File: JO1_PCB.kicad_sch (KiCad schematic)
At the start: 13 parts, among them J1 CN8, J10 ESC_PWM, J11 CAN_WCMCU-1051_BLUEPILL, J2 CN7, J3 CN9, J4 CN10, J5 MPU-6050, J6 CAN_WCMCU-1051_NUCLEO, J7 SERVO, J8 DC_MOTOR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

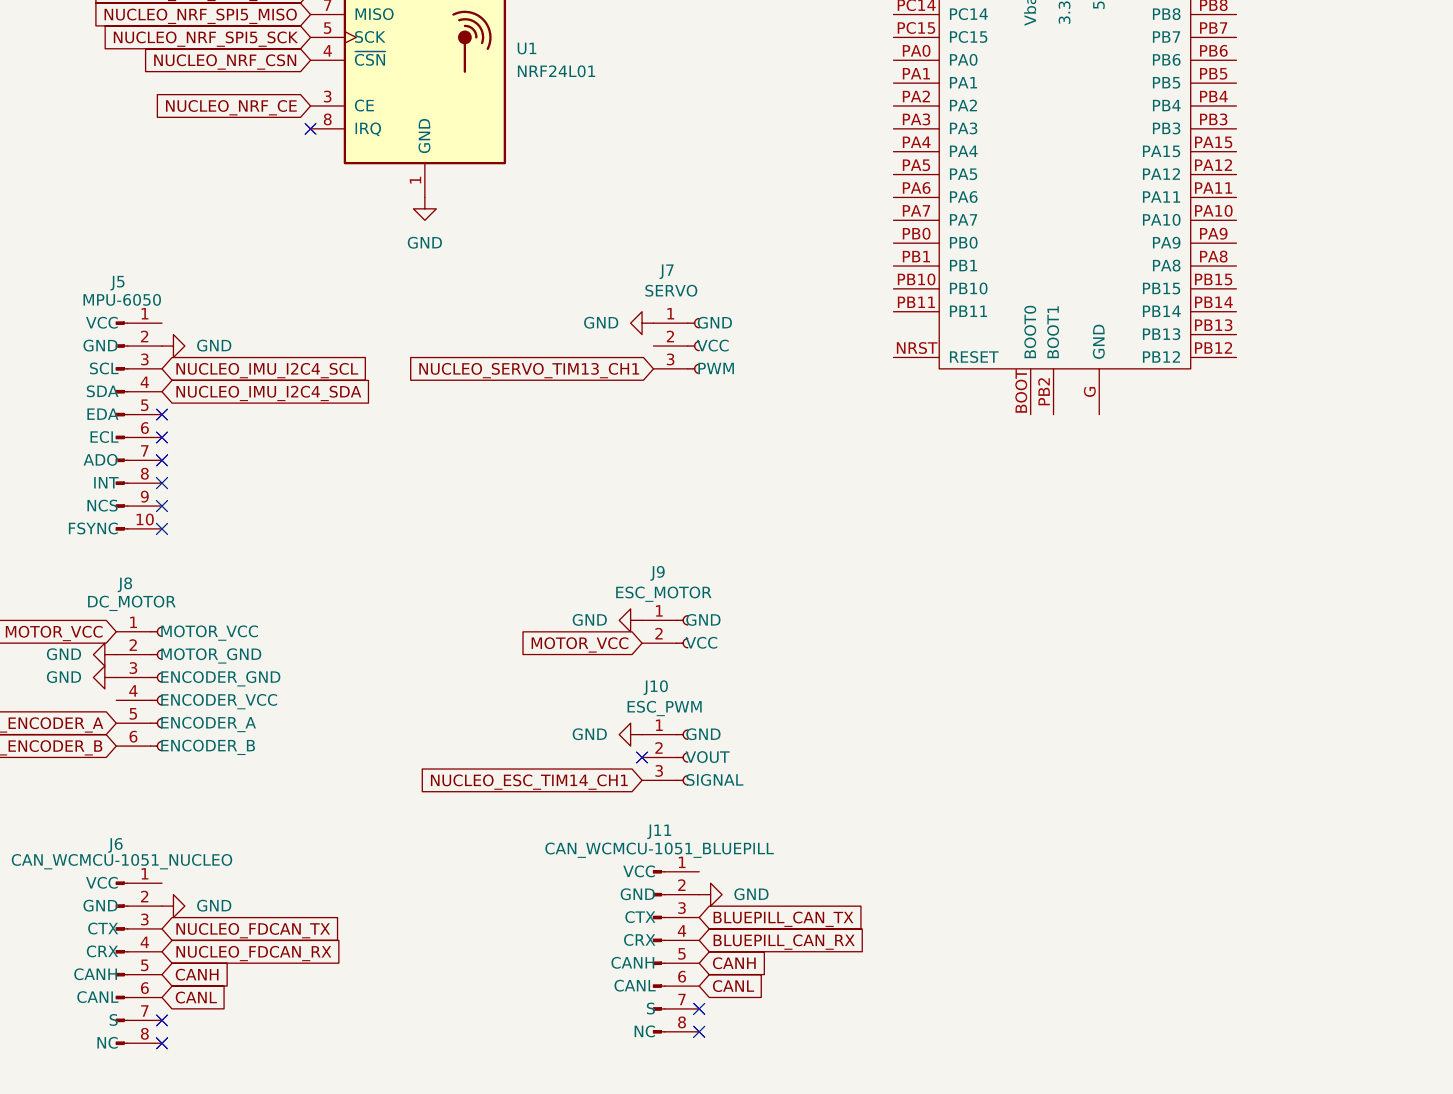
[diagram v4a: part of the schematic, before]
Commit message: Added CAN transceiver for Blue Pill
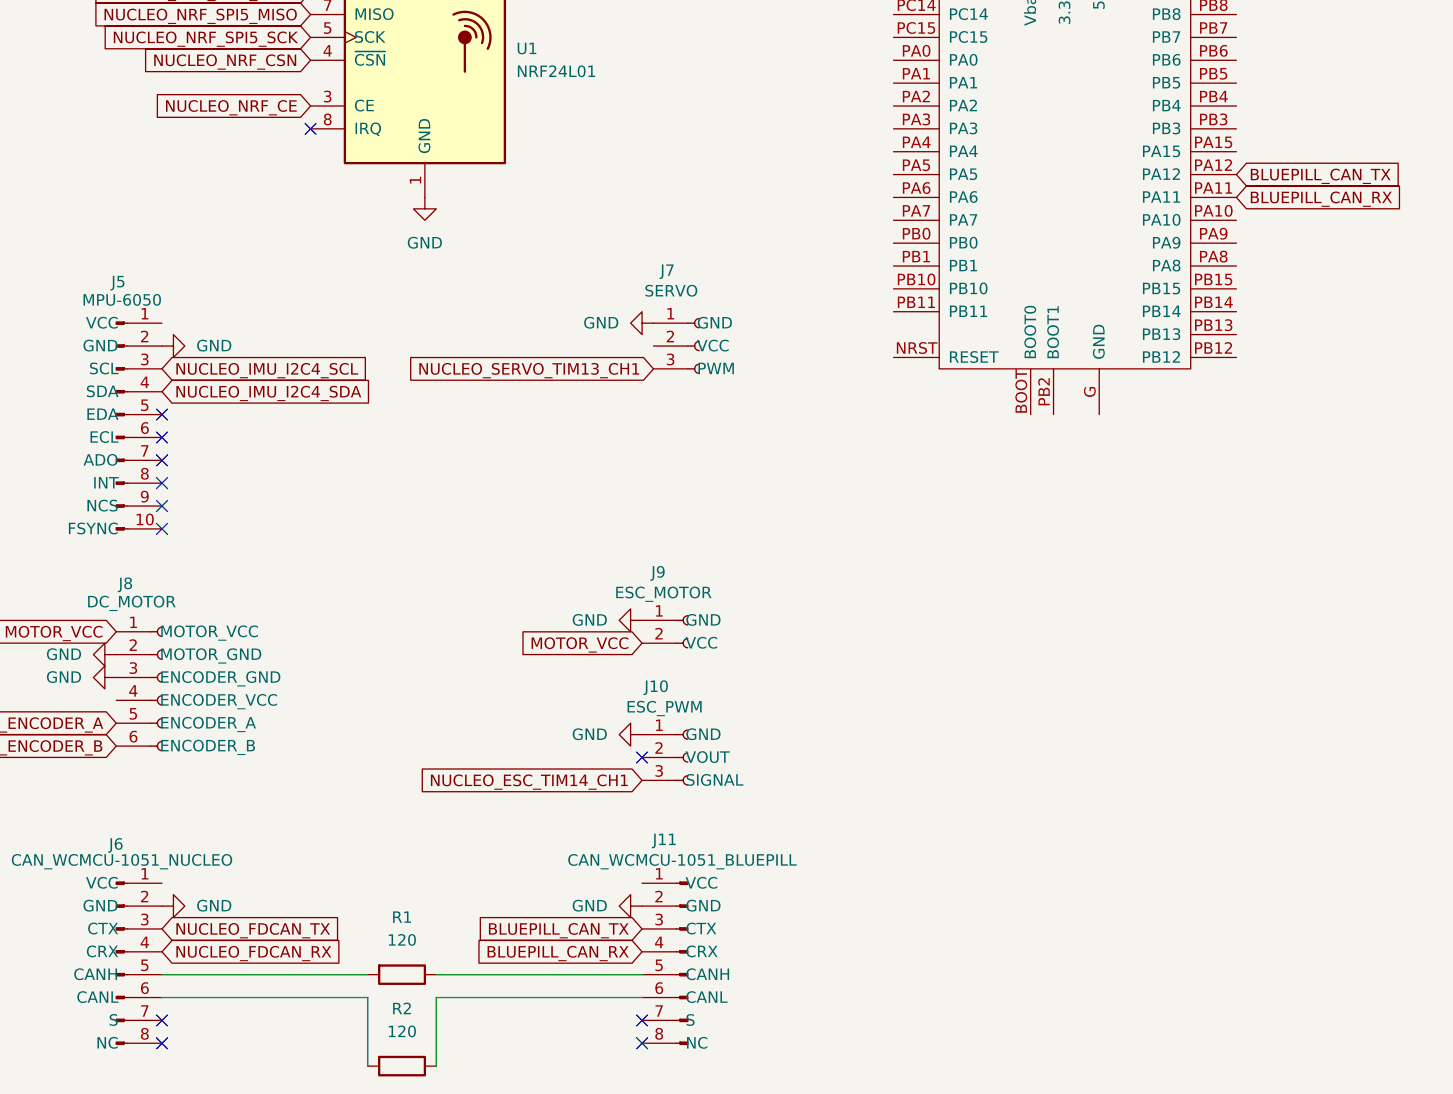
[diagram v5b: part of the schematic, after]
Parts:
- added R1, R2: 120, Resistor_THT:R_Axial_DIN0204_L3.6mm_D1.6mm_P5.08mm_Horizontal, symbol Device:R
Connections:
- net BLUEPILL_CAN_RX: now also U2.PA11
- net BLUEPILL_CAN_TX: now also U2.PA12
- net CANH: no longer names the net of J6.5 (CANH)
- net CANH: now also R1.2; no longer J11.5 (CANH)
- net CANL: no longer names the net of J6.6 (CANL)
- net CANL: now also R2.2; no longer J11.6 (CANL)
- new net: J11.5 (CANH), R1.1
- new net: J11.6 (CANL), R2.1
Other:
- moved on the sheet: J11

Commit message: Placed components
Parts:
- added H1, H2, H3, H4: MountingHole, MountingHole:MountingHole_2.1mm, symbol Mechanical:MountingHole
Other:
- moved on the sheet: U2

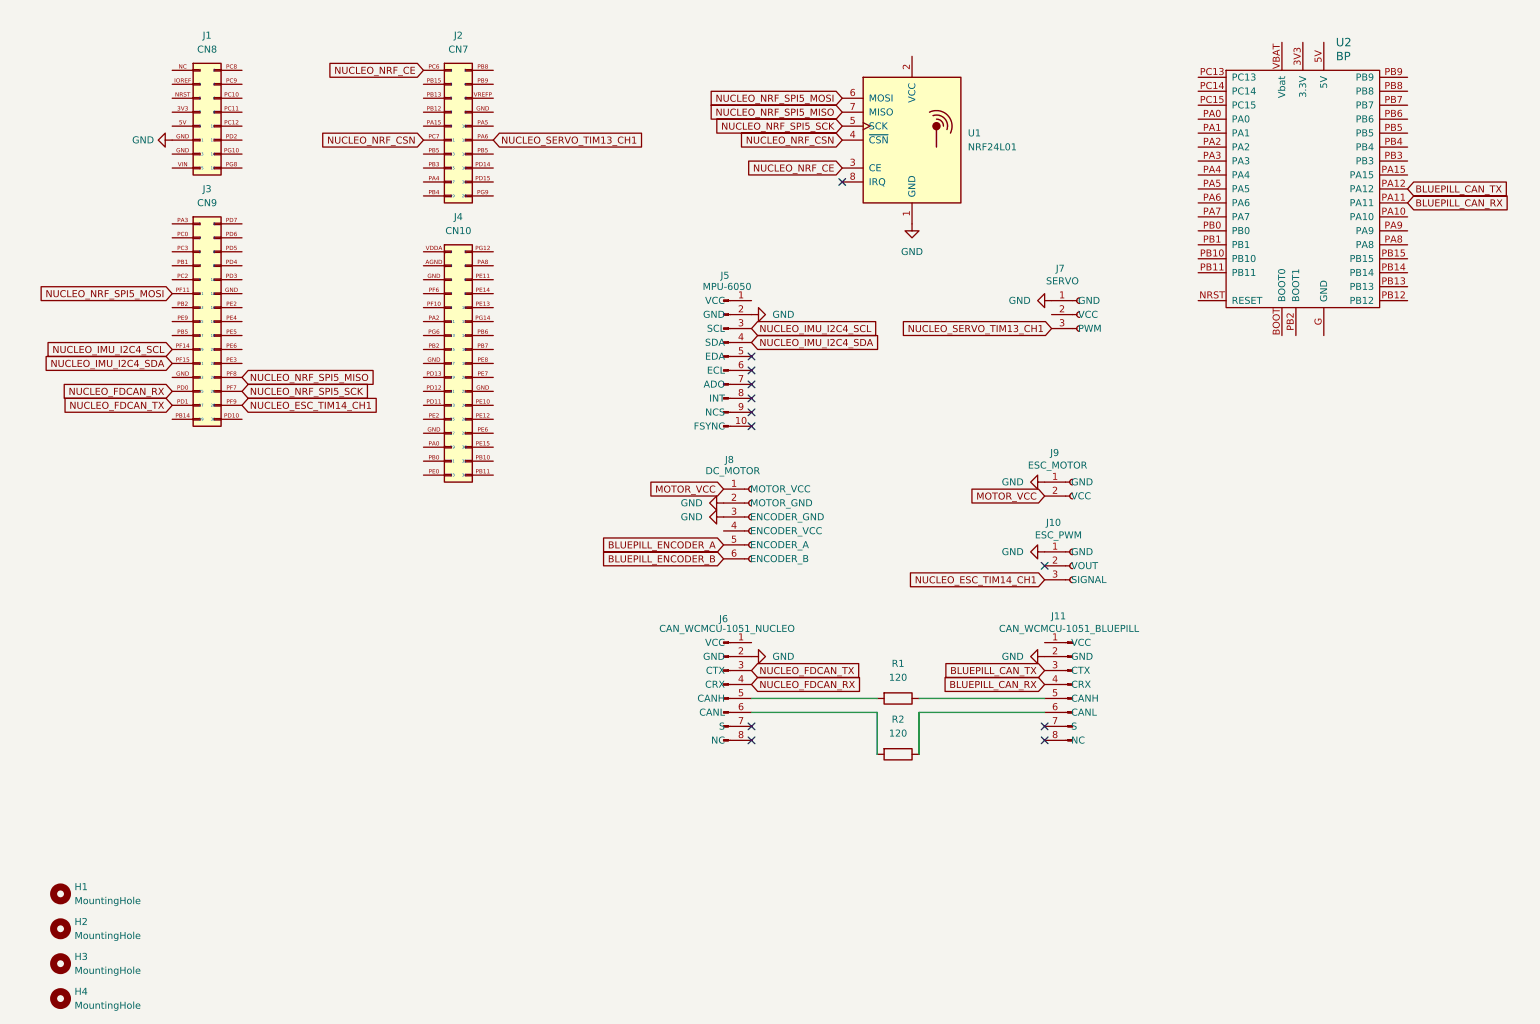
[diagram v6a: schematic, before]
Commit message: Added screw terminals
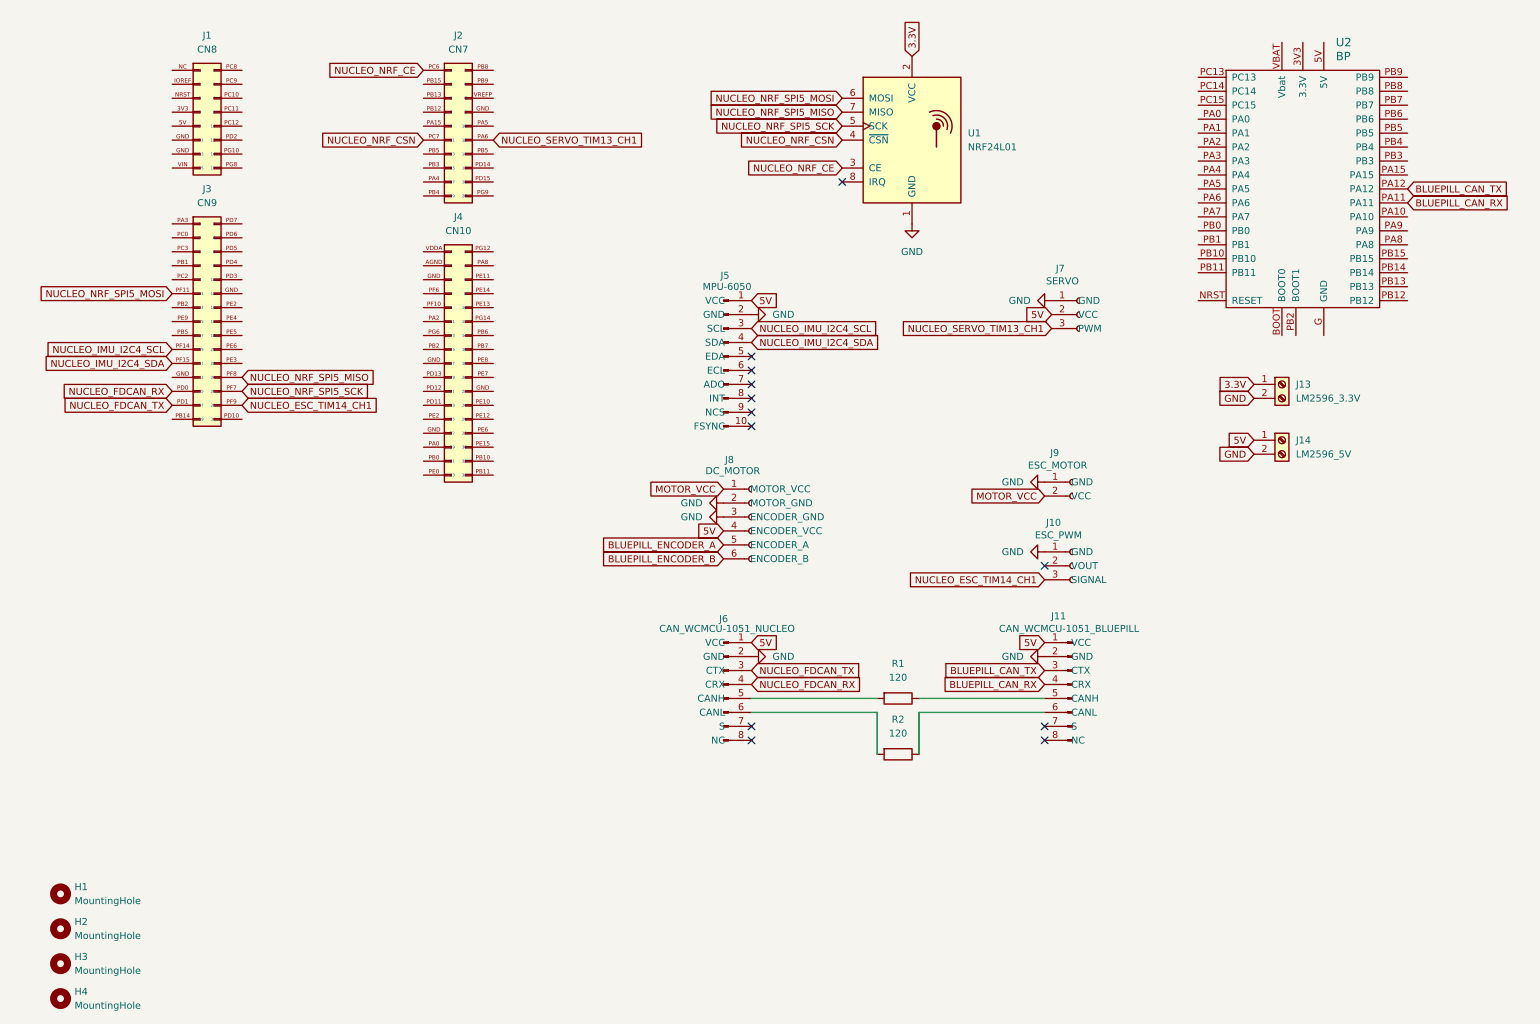
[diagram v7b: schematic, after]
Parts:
- added J13: LM2596_3.3V, symbol Connector:Screw_Terminal_01x02
- added J14: LM2596_5V, symbol Connector:Screw_Terminal_01x02
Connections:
- net GND: now also J13.2 (Pin_2), J14.2 (Pin_2); no longer J1.GND (13)
- net 5V: now reaches J5.1 (VCC)
- net 5V: now also J11.1 (VCC), J6.1 (VCC), J7.2 (VCC), J8.4 (ENCODER_VCC), J14.1 (Pin_1)
- net 3.3V: now reaches U1.2 (VCC)
- net 3.3V: now also J13.1 (Pin_1)

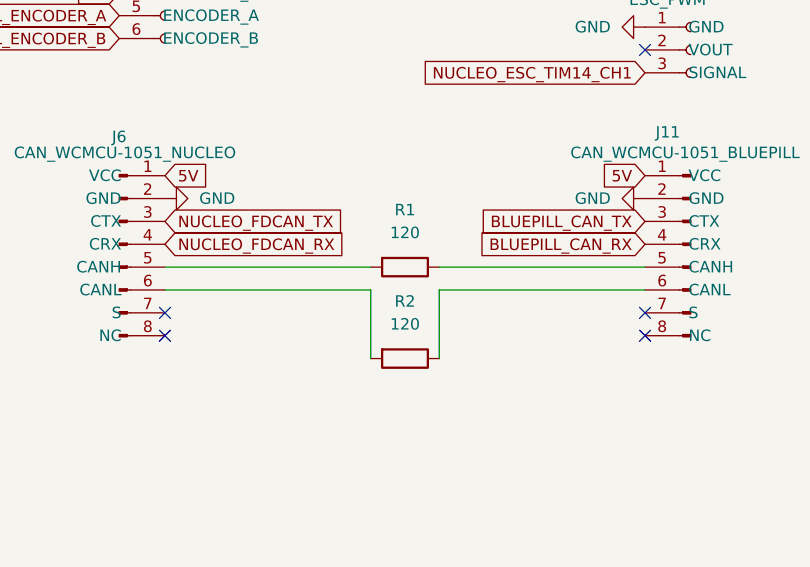
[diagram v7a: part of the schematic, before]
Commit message: Corrected CAN bus
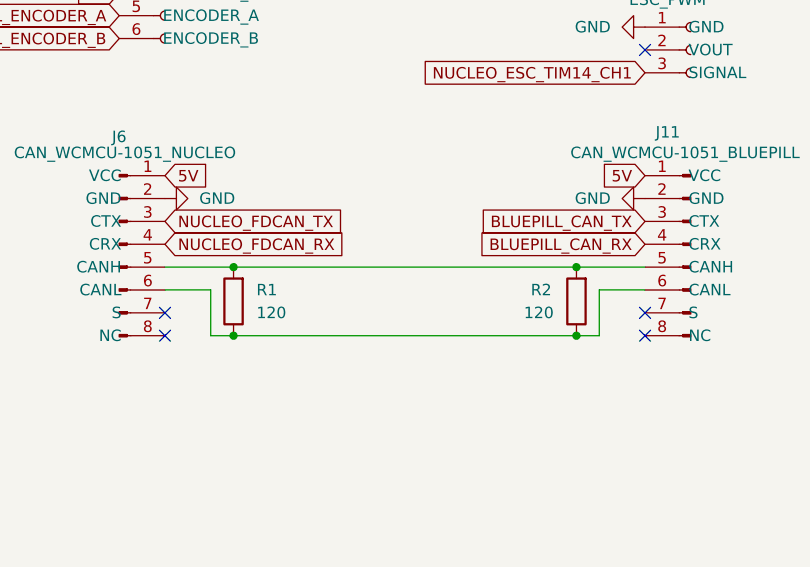
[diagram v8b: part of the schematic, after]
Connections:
- net at J6.5 (CANH), R1.2: now also J11.5 (CANH), R2.2
- net at J6.6 (CANL): now also J11.6 (CANL), R1.1, R2.1; no longer R2.2
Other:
- moved on the sheet: R1, R2
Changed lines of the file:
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@@
 	(generator_version "8.0")
 	(paper "A4")
+	(junction
+		(at 151.13 135.89)
+		(diameter 0)
+		(color 0 0 0 0)
+	)
+	(junction
+		(at 151.13 143.51)
+		(diameter 0)
+		(color 0 0 0 0)
+	)
+	(junction
+		(at 189.23 135.89)
+		(diameter 0)
+		(color 0 0 0 0)
+	)
+	(junction
+		(at 189.23 143.51)
+		(diameter 0)
+		(color 0 0 0 0)
+	)
 	(no_connect
 		(at 143.51 143.51)
@@
 	(wire
 		(pts
-			(xy 173.99 138.43) (xy 196.85 138.43)
+			(xy 189.23 143.51) (xy 191.77 143.51)
+		)
+		(stroke
+			(width 0)
+			(type default)
+		)
+	)
+	(wire
+		(pts
+			(xy 191.77 138.43) (xy 191.77 143.51)
+		)
+		(stroke
+			(width 0)
+			(type default)
+		)
+	)
+	(wire
+		(pts
+			(xy 143.51 138.43) (xy 148.59 138.43)
+		)
+		(stroke
+			(width 0)
+			(type default)
+		)
+	)
+	(wire
+		(pts
+			(xy 151.13 135.89) (xy 189.23 135.89)
 		)
 		(stroke
@@
 	(wire
 		(pts
-			(xy 166.37 138.43) (xy 166.37 146.05)
+			(xy 148.59 143.51) (xy 151.13 143.51)
 		)
 		(stroke
@@
 	(wire
 		(pts
-			(xy 173.99 146.05) (xy 173.99 138.43)
+			(xy 148.59 138.43) (xy 148.59 143.51)
 		)
 		(stroke
@@
 	(wire
 		(pts
-			(xy 143.51 135.89) (xy 166.37 135.89)
+			(xy 151.13 143.51) (xy 189.23 143.51)
 		)
 		(stroke
@@
 	(wire
 		(pts
-			(xy 173.99 135.89) (xy 196.85 135.89)
+			(xy 189.23 135.89) (xy 196.85 135.89)
 		)
 		(stroke
@@
 	(wire
 		(pts
-			(xy 143.51 138.43) (xy 166.37 138.43)
+			(xy 196.85 138.43) (xy 191.77 138.43)
+		)
+		(stroke
+			(width 0)
+			(type default)
+		)
+	)
+	(wire
+		(pts
+			(xy 143.51 135.89) (xy 151.13 135.89)
 		)
 		(stroke
@@
 	(symbol
 		(lib_id "Device:R")
-		(at 170.18 135.89 270)
+		(at 151.13 139.7 180)
 		(unit 1)
 		(exclude_from_sim no)
@@
 		(fields_autoplaced yes)
 		(property "Reference" "R1"
-			(at 170.18 129.54 90)
+			(at 153.67 138.4299 0)
 			(effects
 				(font
 					(size 1.27 1.27)
 				)
+				(justify right)
 			)
 		)
 		(property "Value" "120"
-			(at 170.18 132.08 90)
+			(at 153.67 140.9699 0)
 			(effects
 				(font
 					(size 1.27 1.27)
 				)
+				(justify right)
 			)
 		)
 		(property "Footprint" "Resistor_THT:R_Axial_DIN0204_L3.6mm_D1.6mm_P5.08mm_Horizontal"
-			(at 170.18 134.112 90)
+			(at 152.908 139.7 90)
 			(effects
 				(font
@@
 		)
 		(property "Datasheet" "~"
-			(at 170.18 135.89 0)
+			(at 151.13 139.7 0)
 			(effects
 				(font
@@
 		)
 		(property "Description" "Resistor"
-			(at 170.18 135.89 0)
+			(at 151.13 139.7 0)
 			(effects
 				(font
@@
 	(symbol
 		(lib_id "Device:R")
-		(at 170.18 146.05 270)
+		(at 189.23 139.7 180)
 		(unit 1)
 		(exclude_from_sim no)
@@
 		(on_board yes)
 		(dnp no)
-		(fields_autoplaced yes)
 		(property "Reference" "R2"
-			(at 170.18 139.7 90)
+			(at 184.15 138.43 0)
 			(effects
 				(font
 					(size 1.27 1.27)
 				)
+				(justify right)
 			)
 		)
 		(property "Value" "120"
-			(at 170.18 142.24 90)
+			(at 183.388 140.97 0)
 			(effects
 				(font
 					(size 1.27 1.27)
 				)
+				(justify right)
 			)
 		)
 		(property "Footprint" "Resistor_THT:R_Axial_DIN0204_L3.6mm_D1.6mm_P5.08mm_Horizontal"
-			(at 170.18 144.272 90)
+			(at 191.008 139.7 90)
 			(effects
 				(font
@@
 		)
 		(property "Datasheet" "~"
-			(at 170.18 146.05 0)
+			(at 189.23 139.7 0)
 			(effects
 				(font
@@
 		)
 		(property "Description" "Resistor"
-			(at 170.18 146.05 0)
+			(at 189.23 139.7 0)
 			(effects
 				(font
